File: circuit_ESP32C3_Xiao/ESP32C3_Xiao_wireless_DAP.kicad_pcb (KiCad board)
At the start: 2 copper layers, 70 x 35 mm, 39 parts, among them J1 Cortex Debug 10pin connector, J2 ARM Standard JTAG, J3 Cortex Debug 10pin connector, J4 Conn_01x02, J6 Serial, Q1 ZXM61N03F, U1 XIAO-ESP32-C3-SMD, U2 AP1117-ADJ

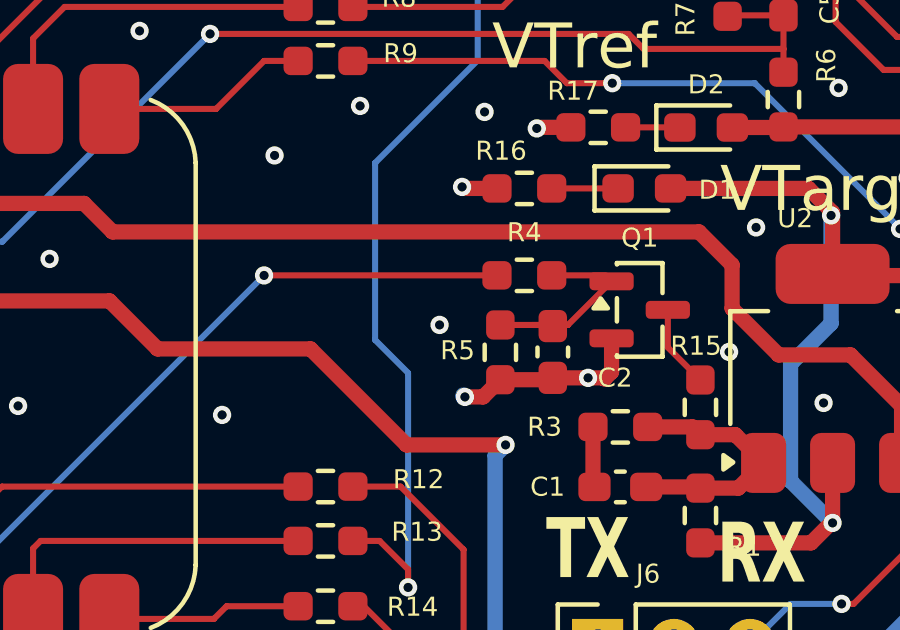
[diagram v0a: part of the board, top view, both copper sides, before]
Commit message: Update the circuit, and create proper SPICE simulation model.
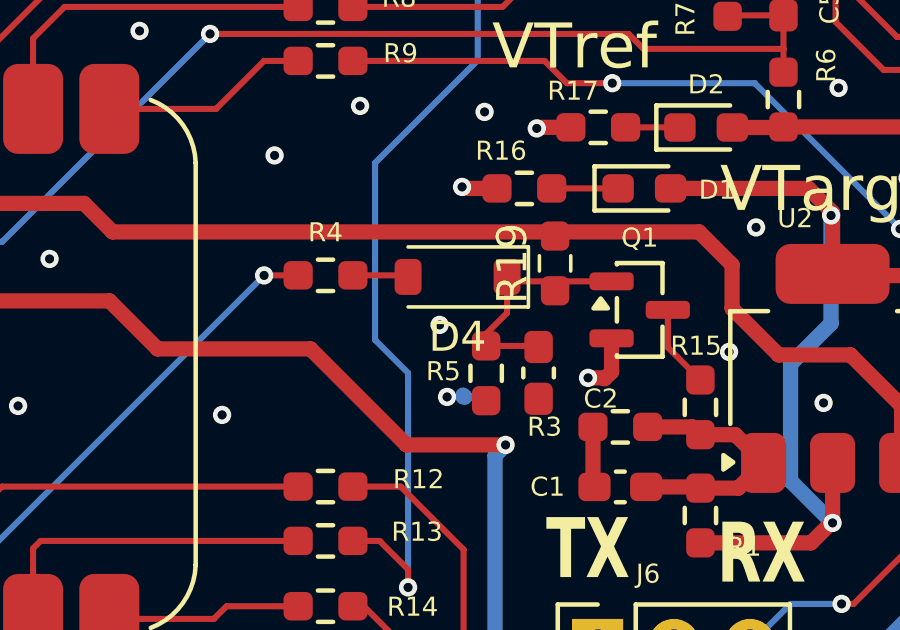
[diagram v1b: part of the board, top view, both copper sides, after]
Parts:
- added D4: 1N4148W, Diode_SMD:D_SOD-123, F.Cu at (129.2, 81.4)
- added R19: 220k, Resistor_SMD:R_0603_1608Metric_Pad0.98x0.95mm_HandSolder, F.Cu at (132.4, 81.0)
- Q1: value ZXM61N03F -> YJL2304A
- R15: value 3.9k -> 39
- R3: value 100k -> 27k
- R4: value 1k -> 39k
- R5: value 22k -> 10k
- moved R4 6.63 mm to (124.8, 81.4)
- moved R5 0.84 mm to (130.1, 84.6)
- moved C2 0.84 mm to (131.9, 84.6)
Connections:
- C2 pad 1: Net-(Q1-G) -> /INPut
- Q1 pad 1: Net-(Q1-G) -> /INPut
- R4 pad 2: Net-(Q1-G) -> Net-(D4-A)
- R5 pad 2: Net-(Q1-G) -> /INPut
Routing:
- net /INPut: track 0.00 -> 7.90 mm
- net Net-(Q1-G): track 6.73 -> 0.00 mm
- net /VTarget_PWM: track 32.1 -> 25.5 mm
- net GND: track 59.8 -> 55.4 mm
- net Net-(D4-A): track 0.00 -> 1.86 mm

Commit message: kicad: update ESP32C3 XIAO design + fabrication outputs
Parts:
- added G***: LOGO, LOGO, B.Cu at (105.0, 74.5)
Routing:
- net /TCK/SWDCLK: track 94.2 -> 90.5 mm
- net /nRST: track 68.5 -> 65.5 mm
- net /VCOM_TX: track 76.1 -> 73.3 mm
- net /nTRST: track 68.5 -> 67.3 mm
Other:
- board text added: "10-PIN CORTEX DEBUG (J1/J3)"
- board text added: "13:TDO 14:GND 15:nRST 16:GND 17:RX 18:GND"
- board text added: "19:VTarget 20:VTref (TX:11 RX:17)"
- board text added: "1:VTref 2:VTref 3:nTRST 4:GND 5:TDI 6:GND"
- board text added: "20-PIN ARM JTAG (J2)"
- board text added: "7:TMS 8:GND 9:TCK 10:GND 11:TX 12:GND"
- board text added: "Pin 1: VTref Pin 2: TMS/SWDIO"
- board text added: "Pin 3: GND Pin 4: TCK/SWCLK"
- board text added: "Pin 5: UART_TX Pin 6: TDO/SWO"
- board text added: "Pin 7: UART_RX Pin 8: TDI"
- board text added: "Pin 9: VTarget Pin 10: nRST"
